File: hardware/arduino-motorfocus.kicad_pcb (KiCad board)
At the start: 2 copper layers, 52 x 61 mm, 23 parts, among them J1 Motor, J2 PWR_MOTOR, J3 Debug, J4 I2C, J5 STEPS, J6 ULN2003A, J7 PWR_MOTOR, SW1 IN, SW2 OUT, SW3 WIN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

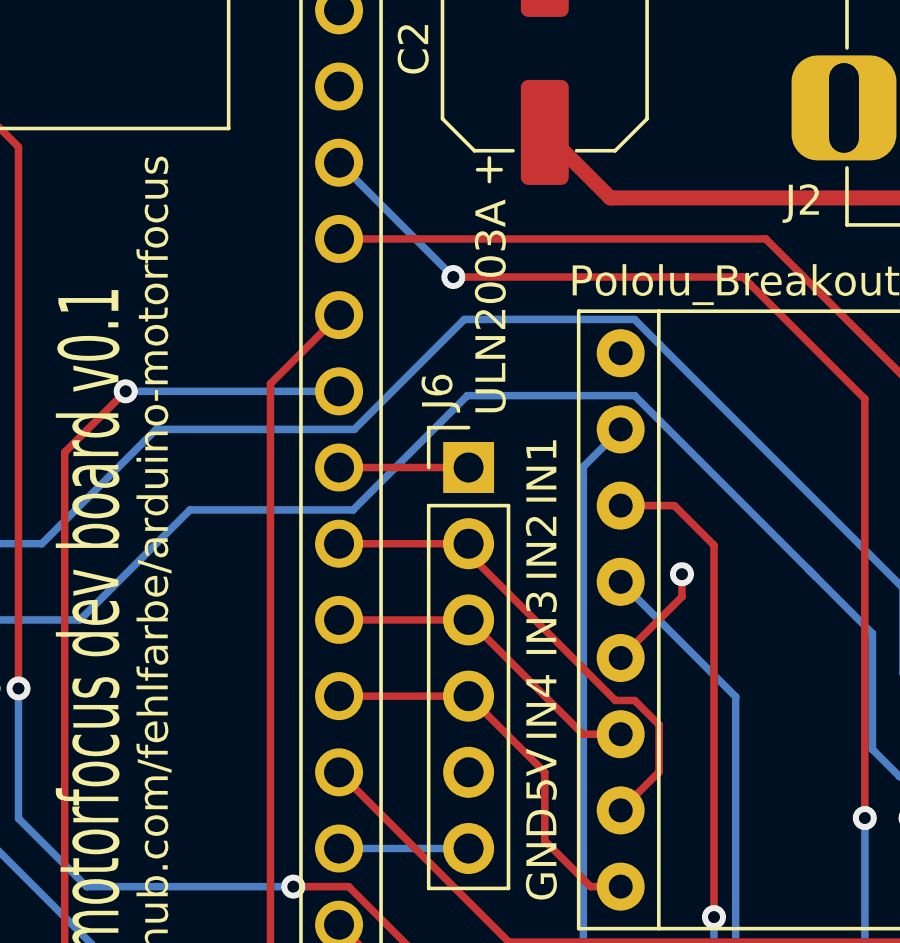
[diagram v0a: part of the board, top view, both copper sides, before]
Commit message: Added simple PCB project and doc
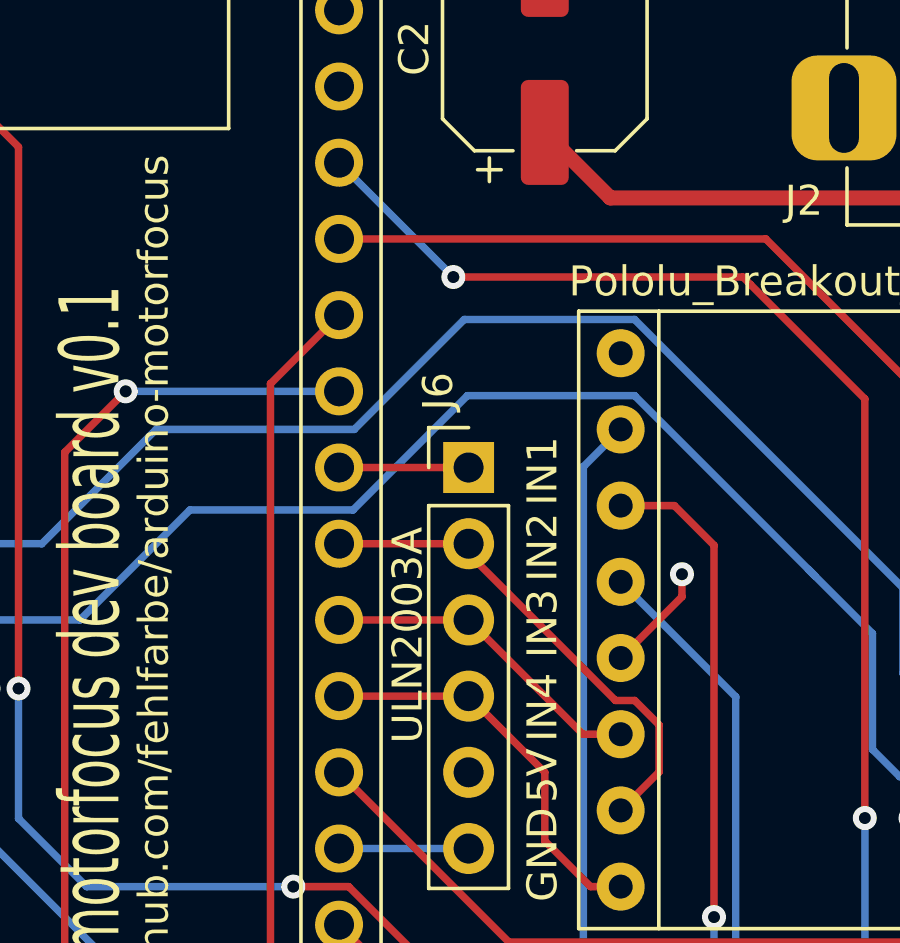
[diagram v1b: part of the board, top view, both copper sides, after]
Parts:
- C2: value C_Polarized -> 100uF
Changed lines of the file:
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@@
         (effects (font (size 1 1) (thickness 0.15)))
     )
-    (fp_text value "C_Polarized" (at 0 4.35 90) (layer "F.Fab")
+    (fp_text value "100uF" (at 0 4.35 90) (layer "F.Fab")
         (effects (font (size 1 1) (thickness 0.15)))
     )
@@
         (effects (font (size 1 1) (thickness 0.15)))
     )
-    (fp_text value "ULN2003A" (at 0.762 -5.334 90) (layer "F.SilkS")
-        (effects (font (size 1 1) (thickness 0.15)))
-    )
+    (fp_text value "ULN2003A" (at -2.032 5.588 90) (layer "F.SilkS")
+        (effects (font (size 1 1) (thickness 0.15)))
+    )
